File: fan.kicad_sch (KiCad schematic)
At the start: 10 parts, among them J6 Conn_01x04, Q1 MMBT3904, U10 EMC2101

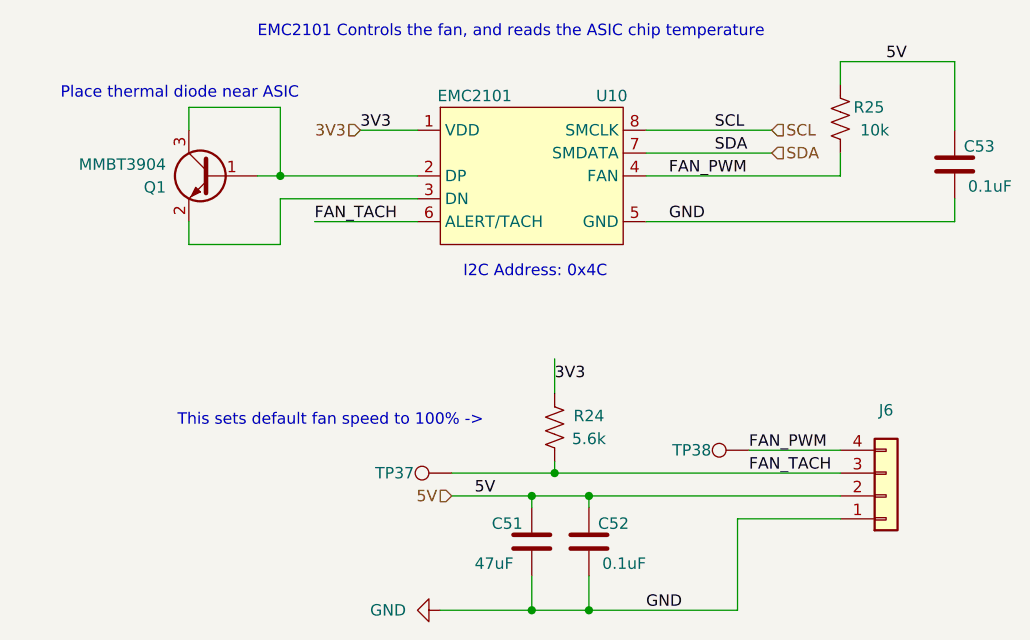
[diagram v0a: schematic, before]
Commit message: fix off-grid and unconnected erc warnings
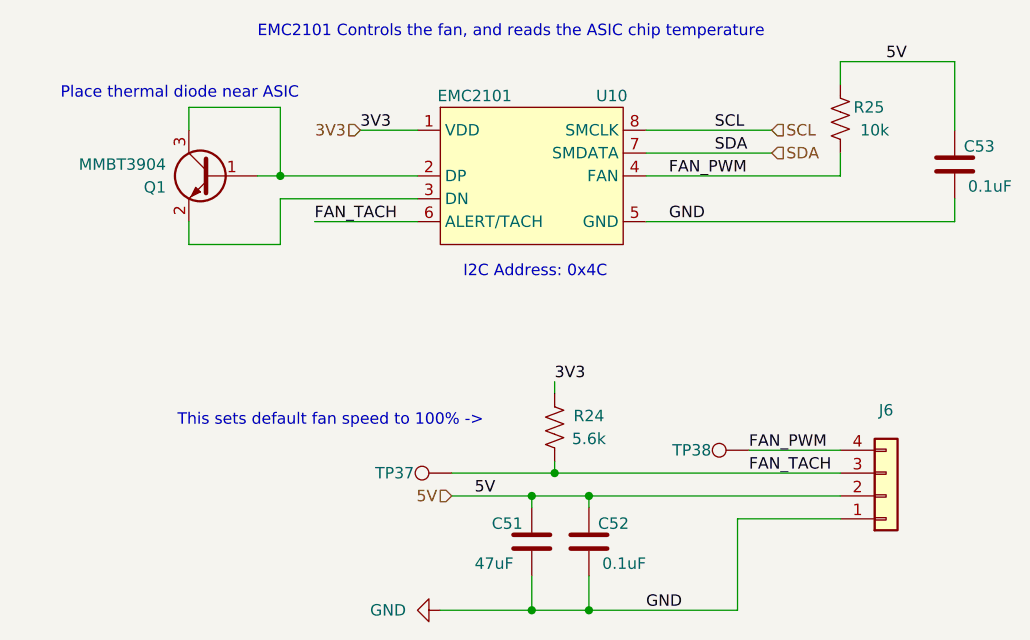
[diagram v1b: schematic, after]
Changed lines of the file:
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@@
+	(wire
+		(pts
+			(xy 147.32 101.6) (xy 147.32 102.87)
+		)
+		(stroke
+			(width 0)
+			(type default)
+		)
+	)
 	(wire
 		(pts
@@
 		)
 		(stroke
-			(width 0)
-			(type default)
-		)
-	)
-	(wire
-		(pts
-			(xy 147.32 99.06) (xy 147.32 102.87)
-		)
-		(stroke
